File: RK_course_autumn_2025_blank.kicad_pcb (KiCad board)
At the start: 2 copper layers, 65 x 80 mm, 13 parts, among them J1 JST-ZH 6pin, J2 JST-ZH 6pin, J3 Conn_01x02, J4 JST-ZH 6pin, J5 JST-ZH 6pin

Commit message: update
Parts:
- A2: footprint KURSUS:ESP32-S3-DevKitC-1 -> RK_COURSE:ESP32-S3-DevKitC-1
- moved U4 24.7 mm to (99.5, 83.3), turned to -90 degrees
- moved U5 11.8 mm to (98.1, 137.6)
- moved U6 4.42 mm to (81.4, 117.1)
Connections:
- A2 pad 32: unconnected-(A2-38-Pad32) -> MOT3DIR1
- A2 pad 33: unconnected-(A2-37-Pad33) -> MOT3DIR2
- A2 pad 34: unconnected-(A2-36-Pad34) -> MOT3SPEED
- A2 pad 35: unconnected-(A2-Pad35) -> MOT4DIR1
- A2 pad 36: unconnected-(A2-0-Pad36) -> MOT4DIR2
- A2 pad 37: unconnected-(A2-45-Pad37) -> MOT4SPEED

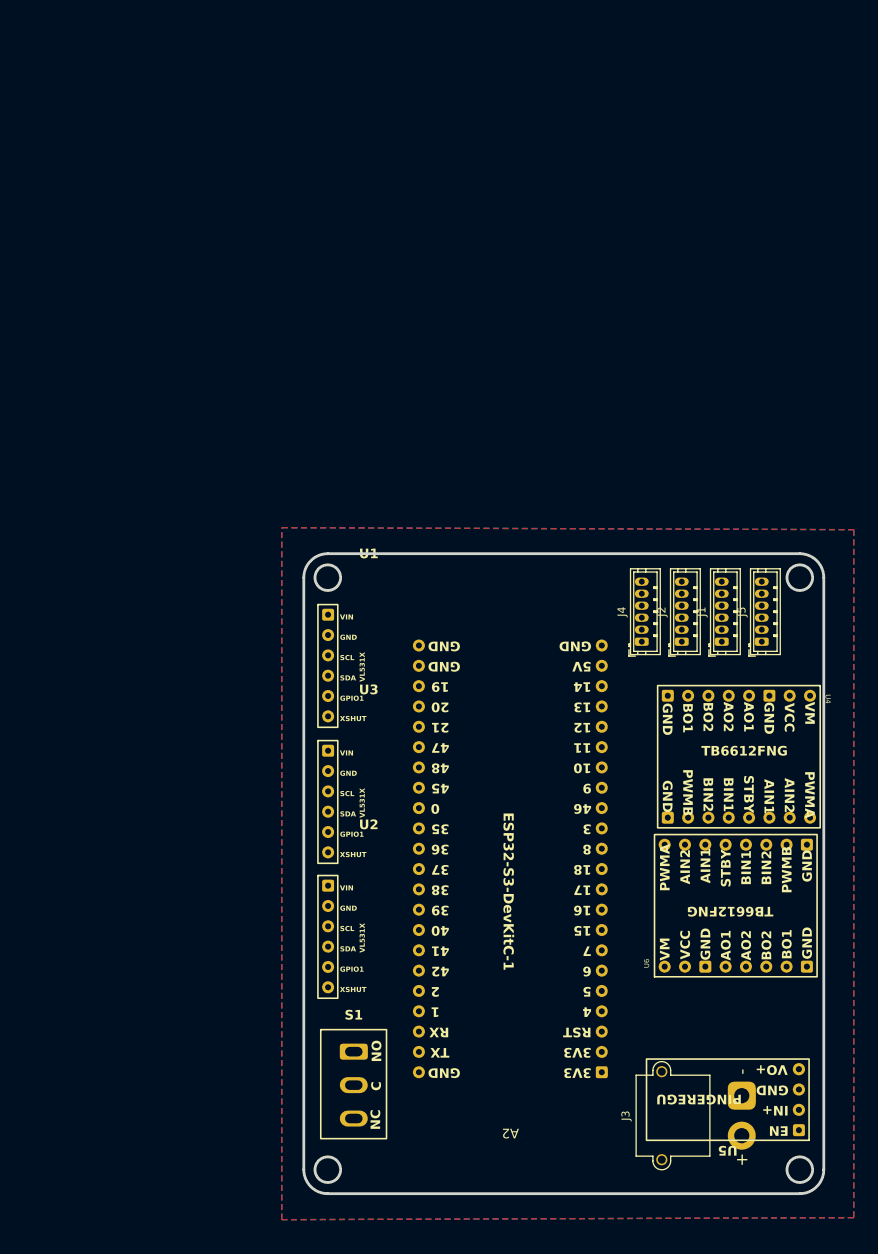
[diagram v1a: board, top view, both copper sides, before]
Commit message: Added IMU footprint, model, schematic. Updated the schematic and PCB a bit
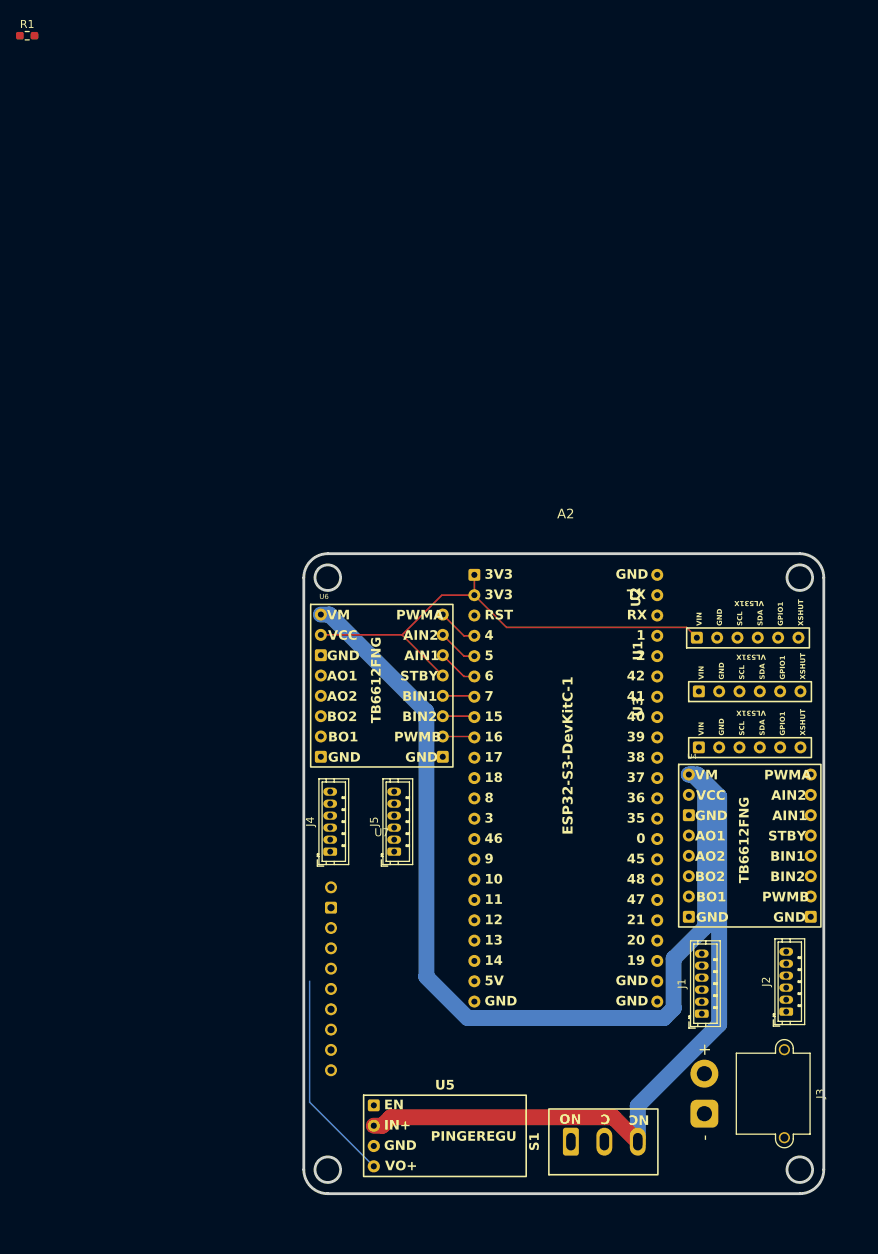
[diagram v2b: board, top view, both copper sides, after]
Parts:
- added R1: R, Resistor_SMD:R_0603_1608Metric_Pad0.98x0.95mm_HandSolder, F.Cu at (1.68, 0.76)
- added U7: ~, KURSUS:IMU, F.Cu at (46.0, 100.9)
- J1, J2, J4, J5: footprint Connector_JST:JST_ZH_B6B-ZR_1x06_P1.50mm_Vertical -> KURSUS:JST_ZH_B6B-ZR_1x06_P1.50mm_Vertical
- J3: footprint Connector_AMASS:AMASS_XT30PW-M_1x02_P2.50mm_Horizontal -> KURSUS:AMASS_XT30PW-M_1x02_P2.50mm_Horizontal
- moved A2 62.6 mm to (69.0, 68.1), turned to 0 degrees
- moved U6 61.5 mm to (38.4, 73.1), turned to 0 degrees
- moved U5 53.2 mm to (45.0, 134.5), turned to 0 degrees
- moved J5 52.9 mm to (47.5, 102.8)
- moved J2 48.1 mm to (96.5, 122.8)
- moved J4 47.0 mm to (39.5, 102.8)
- moved J1 46.6 mm to (86.0, 123.0)
- moved U2 43.9 mm to (77.8, 70.9), turned to 90 degrees
- moved U1 35.8 mm to (78.0, 77.6), turned to 90 degrees
- moved U3 33.7 mm to (78.0, 84.6), turned to 90 degrees
- moved S1 29.4 mm to (69.6, 139.0), turned to 90 degrees
- moved U4 18.1 mm to (84.4, 93.1), turned to 0 degrees
- moved J3 5.19 mm to (86.3, 135.5), turned to -90 degrees
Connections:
- A2 pad 10: XSHUT1 -> unconnected-(A2-17-Pad10)
- A2 pad 11: XSHUT2 -> unconnected-(A2-18-Pad11)
- A2 pad 12: XSHUT3 -> unconnected-(A2-8-Pad12)
- A2 pad 13: unconnected-(A2-3-Pad13) -> INT
- A2 pad 32: MOT3DIR1 -> XSHUT3
- A2 pad 33: MOT3DIR2 -> XSHUT2
- A2 pad 34: MOT3SPEED -> XSHUT1
- A2 pad 35: MOT4DIR1 -> unconnected-(A2-Pad35)
- A2 pad 36: MOT4DIR2 -> unconnected-(A2-0-Pad36)
- A2 pad 37: MOT4SPEED -> unconnected-(A2-45-Pad37)
- A2 pad 4: unconnected-(A2-Pad4) -> MOT3SPEED
- A2 pad 5: SDA -> MOT3DIR1
- A2 pad 6: SCL -> MOT3DIR2
- A2 pad 7: unconnected-(A2-Pad7) -> MOT4DIR1
- A2 pad 8: unconnected-(A2-15-Pad8) -> MOT4DIR2
- A2 pad 9: unconnected-(A2-16-Pad9) -> MOT4SPEED
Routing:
- net +12V: track 0.00 -> 203.9 mm
- net +3V3: track 0.00 -> 61.0 mm
- net +5V: track 0.00 -> 26.5 mm
- net MOT3DIR1: track 0.00 -> 5.22 mm
- net MOT3SPEED: track 0.00 -> 5.05 mm
- net MOT3DIR2: track 0.00 -> 5.05 mm
- net MOT4SPEED: track 0.00 -> 4.00 mm
- net MOT4DIR1: track 0.00 -> 4.00 mm
- net MOT4DIR2: track 0.00 -> 4.00 mm
- removed copper zone on B.Cu, net GND
- removed copper zone on F.Cu, net GND

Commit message: Better placement for 12V
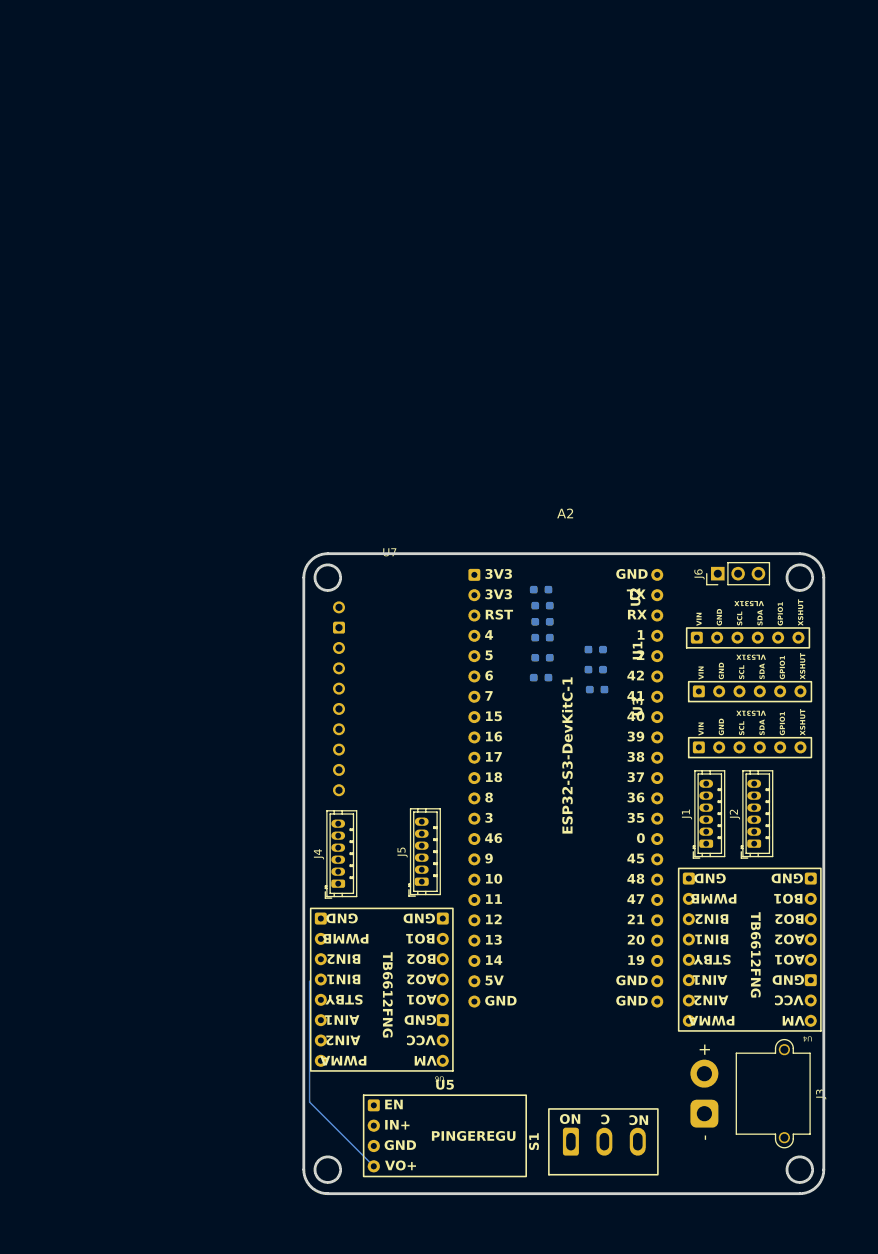
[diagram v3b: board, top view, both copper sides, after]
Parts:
- added J6: Conn_01x03, Connector_PinHeader_2.54mm:PinHeader_1x03_P2.54mm_Vertical, F.Cu at (88.0, 68.0)
- added R2: R, Resistor_SMD:R_0603_1608Metric_Pad0.98x0.95mm_HandSolder, B.Cu at (72.7, 77.5)
- added R3: R, Resistor_SMD:R_0603_1608Metric_Pad0.98x0.95mm_HandSolder, B.Cu at (72.7, 80.0)
- added R4: 5000, Resistor_SMD:R_0603_1608Metric_Pad0.98x0.95mm_HandSolder, B.Cu at (65.9, 81.0)
- added R5: 10000, Resistor_SMD:R_0603_1608Metric_Pad0.98x0.95mm_HandSolder, B.Cu at (66.1, 72.0)
- added R6: 10000, Resistor_SMD:R_0603_1608Metric_Pad0.98x0.95mm_HandSolder, B.Cu at (66.1, 74.0)
- added R7: 5000, Resistor_SMD:R_0603_1608Metric_Pad0.98x0.95mm_HandSolder, B.Cu at (66.1, 76.0)
- added R8: 10000, Resistor_SMD:R_0603_1608Metric_Pad0.98x0.95mm_HandSolder, B.Cu at (65.9, 70.0)
- added R9: 5000, Resistor_SMD:R_0603_1608Metric_Pad0.98x0.95mm_HandSolder, B.Cu at (66.1, 78.5)
- R1: moved to B.Cu
- moved R1 108.4 mm to (72.9, 82.5), turned to 180 degrees
- moved U6 57.8 mm to (53.6, 128.9), turned to 180 degrees
- moved U7 35.0 mm to (47.0, 65.9)
- moved U4 34.3 mm to (99.6, 123.9), turned to 180 degrees
- moved J2 21.4 mm to (92.5, 101.8)
- moved J1 21.3 mm to (86.5, 101.8)
- moved J5 5.10 mm to (51.0, 106.5)
- moved J4 4.12 mm to (40.5, 106.8)
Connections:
- A2 pad 14: unconnected-(A2-46-Pad14) -> SDA
- A2 pad 15: unconnected-(A2-9-Pad15) -> SCL
- A2 pad 22: GND -> XSHUT1
- A2 pad 23: GND -> XSHUT1
- A2 pad 32: XSHUT3 -> XSHUT1
- A2 pad 33: XSHUT2 -> XSHUT1
- A2 pad 43: GND -> XSHUT1
- A2 pad 44: GND -> XSHUT1
- J3 pad 1: GND -> XSHUT1
- R1 pad 1: unconnected-(R1-Pad1) -> +3V3
- R1 pad 2: unconnected-(R1-Pad2) -> XSHUT1
- U1 pad 2: GND -> XSHUT1
- U2 pad 2: GND -> XSHUT1
- U2 pad 6: XSHUT2 -> XSHUT1
- U3 pad 2: GND -> XSHUT1
- U3 pad 6: XSHUT3 -> XSHUT1
- U4 pad 16: GND -> XSHUT1
- U4 pad 3: GND -> XSHUT1
- U4 pad 8: GND -> XSHUT1
- U5 pad 3: GND -> XSHUT1
- U6 pad 16: GND -> XSHUT1
- U6 pad 3: GND -> XSHUT1
- U6 pad 8: GND -> XSHUT1
- U7 pad 10: GND -> XSHUT1
- U7 pad 2: GND -> XSHUT1
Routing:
- net +12V: track 203.9 -> 0.00 mm
- net +3V3: track 61.0 -> 0.00 mm
- net MOT3SPEED: track 5.05 -> 0.00 mm
- net MOT3DIR2: track 5.05 -> 0.00 mm
- net MOT3DIR1: track 5.22 -> 0.17 mm
- net MOT4SPEED: track 4.00 -> 0.17 mm
- net MOT4DIR2: track 4.00 -> 0.17 mm
- net MOT4DIR1: track 4.00 -> 0.17 mm

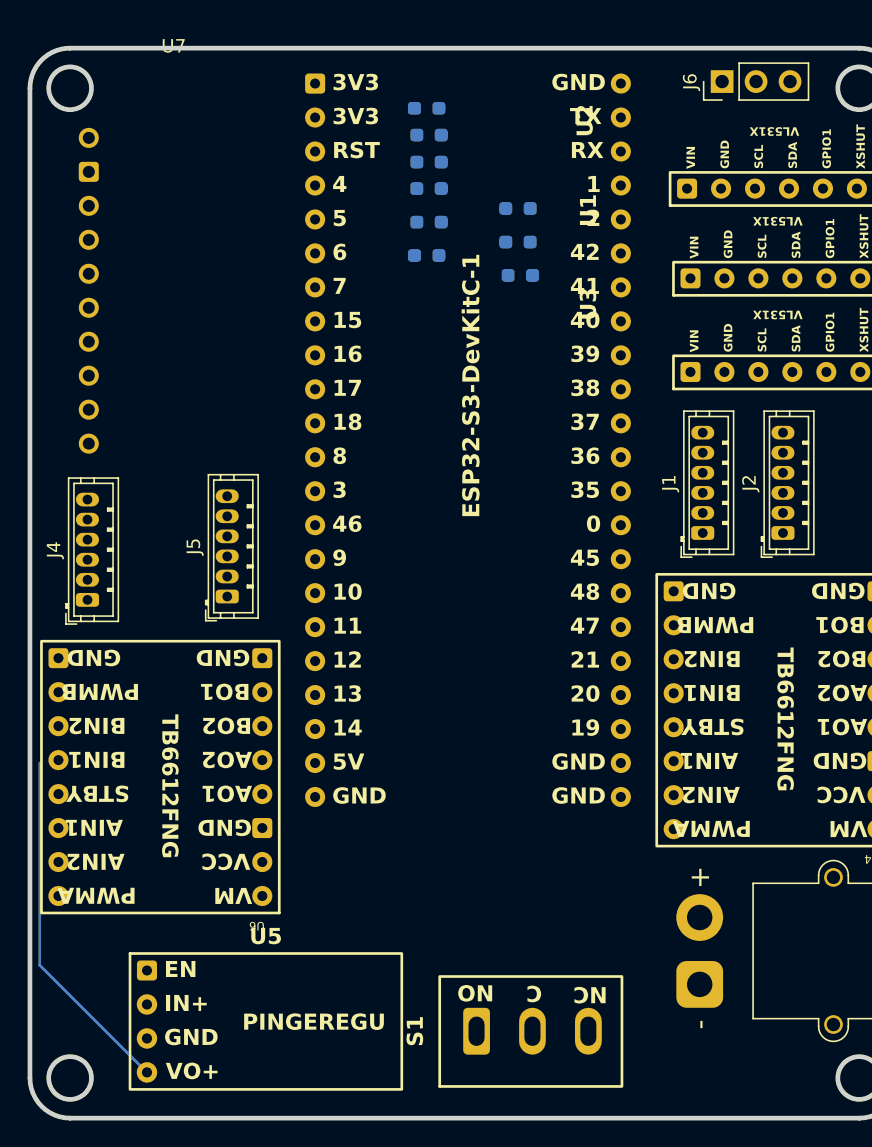
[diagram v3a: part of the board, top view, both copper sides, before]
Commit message: Fixed pull-up resistors, added battery voltage measurement, better pin connection layout
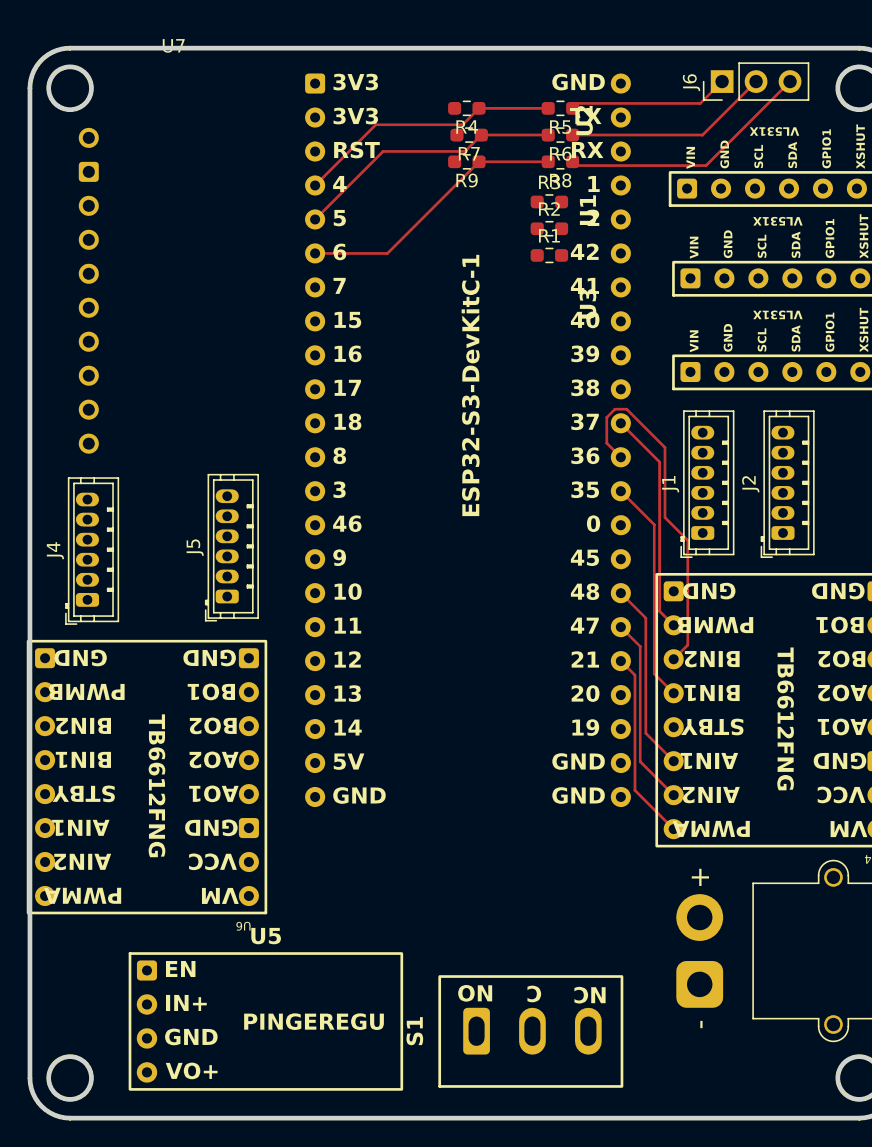
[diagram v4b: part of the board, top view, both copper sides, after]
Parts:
- R1, R2, R3: value R -> 10k; moved to F.Cu
- R4, R7, R9: value 5000 -> 5k; moved to F.Cu
- R5, R6, R8: value 10000 -> 10k; moved to F.Cu
- moved R4 11.4 mm to (68.9, 70.0)
- moved R8 10.8 mm to (75.9, 74.0)
- moved R6 10.0 mm to (75.9, 72.0)
- moved R5 10.0 mm to (75.9, 70.0)
- moved R9 5.32 mm to (68.9, 74.0)
- moved R7 5.00 mm to (69.1, 72.0)
- moved R3 3.81 mm to (75.1, 77.0), turned to 0 degrees
- moved R2 2.79 mm to (75.1, 79.0), turned to 0 degrees
- moved R1 2.64 mm to (75.1, 81.0), turned to 0 degrees
- moved U6 1.00 mm to (52.6, 128.9)
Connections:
- A2 pad 10: unconnected-(A2-17-Pad10) -> INT
- A2 pad 13: INT -> unconnected-(A2-3-Pad13)
- A2 pad 14: SDA -> unconnected-(A2-46-Pad14)
- A2 pad 15: SCL -> MOT4SPEED
- A2 pad 16: unconnected-(A2-10-Pad16) -> MOT4DIR2
- A2 pad 17: unconnected-(A2-11-Pad17) -> MOT4DIR1
- A2 pad 18: unconnected-(A2-12-Pad18) -> MOT3DIR2
- A2 pad 19: unconnected-(A2-13-Pad19) -> MOT3DIR1
- A2 pad 20: unconnected-(A2-14-Pad20) -> MOT3SPEED
- A2 pad 22: XSHUT1 -> GND
- A2 pad 23: XSHUT1 -> GND
- A2 pad 26: MOT1DIR1 -> XSHUT3
- A2 pad 27: MOT1DIR2 -> XSHUT2
- A2 pad 28: MOT1SPEED -> XSHUT1
- A2 pad 29: MOT2DIR1 -> unconnected-(A2-41-Pad29)
- A2 pad 30: MOT2DIR2 -> SCL
- A2 pad 31: MOT2SPEED -> SDA
- A2 pad 32: XSHUT1 -> unconnected-(A2-38-Pad32)
- A2 pad 33: XSHUT1 -> MOT2SPEED
- A2 pad 34: XSHUT1 -> MOT2DIR2
- A2 pad 35: unconnected-(A2-Pad35) -> MOT2DIR1
- A2 pad 38: unconnected-(A2-48-Pad38) -> MOT1DIR2
- A2 pad 39: unconnected-(A2-47-Pad39) -> MOT1DIR1
- A2 pad 4: MOT3SPEED -> aku1
- A2 pad 40: unconnected-(A2-21-Pad40) -> MOT1SPEED
- A2 pad 43: XSHUT1 -> GND
- A2 pad 44: XSHUT1 -> GND
- A2 pad 5: MOT3DIR1 -> aku2
- A2 pad 6: MOT3DIR2 -> aku3
- A2 pad 7: MOT4DIR1 -> unconnected-(A2-Pad7)
- A2 pad 8: MOT4DIR2 -> unconnected-(A2-15-Pad8)
- A2 pad 9: MOT4SPEED -> unconnected-(A2-16-Pad9)
- J3 pad 1: XSHUT1 -> GND
- R2 pad 2: XSHUT1 -> XSHUT2
- R3 pad 2: XSHUT1 -> XSHUT3
- R4 pad 2: XSHUT1 -> GND
- R7 pad 2: XSHUT1 -> GND
- R9 pad 2: XSHUT1 -> GND
- U1 pad 2: XSHUT1 -> GND
- U2 pad 2: XSHUT1 -> GND
- U2 pad 6: XSHUT1 -> XSHUT2
- U3 pad 2: XSHUT1 -> GND
- U3 pad 6: XSHUT1 -> XSHUT3
- U4 pad 16: XSHUT1 -> GND
- U4 pad 3: XSHUT1 -> GND
- U4 pad 8: XSHUT1 -> GND
- U5 pad 3: XSHUT1 -> GND
- U6 pad 16: XSHUT1 -> GND
- U6 pad 3: XSHUT1 -> GND
- U6 pad 8: XSHUT1 -> GND
- U7 pad 10: XSHUT1 -> GND
- U7 pad 2: XSHUT1 -> GND
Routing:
- net +5V: track 26.5 -> 0.00 mm
- net MOT2DIR2: track 0.00 -> 26.2 mm
- net aku3: track 0.00 -> 20.3 mm
- net aku2: track 0.00 -> 20.0 mm
- net aku1: track 0.00 -> 19.8 mm
- net Net-(J6-Pin_3): track 0.00 -> 19.0 mm
- net MOT2SPEED: track 0.00 -> 16.7 mm
- net MOT2DIR1: track 0.00 -> 16.7 mm
- net Net-(J6-Pin_2): track 0.00 -> 15.4 mm
- net MOT1DIR2: track 0.00 -> 14.2 mm
- net MOT1DIR1: track 0.00 -> 14.2 mm
- net MOT1SPEED: track 0.00 -> 14.2 mm
- net Net-(J6-Pin_1): track 0.00 -> 12.0 mm
